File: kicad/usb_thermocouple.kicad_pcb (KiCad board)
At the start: 2 copper layers, 72 x 47.5 mm, 6 parts, among them U1 SeeeduinoXIAO, U2 ADA_MAX31855

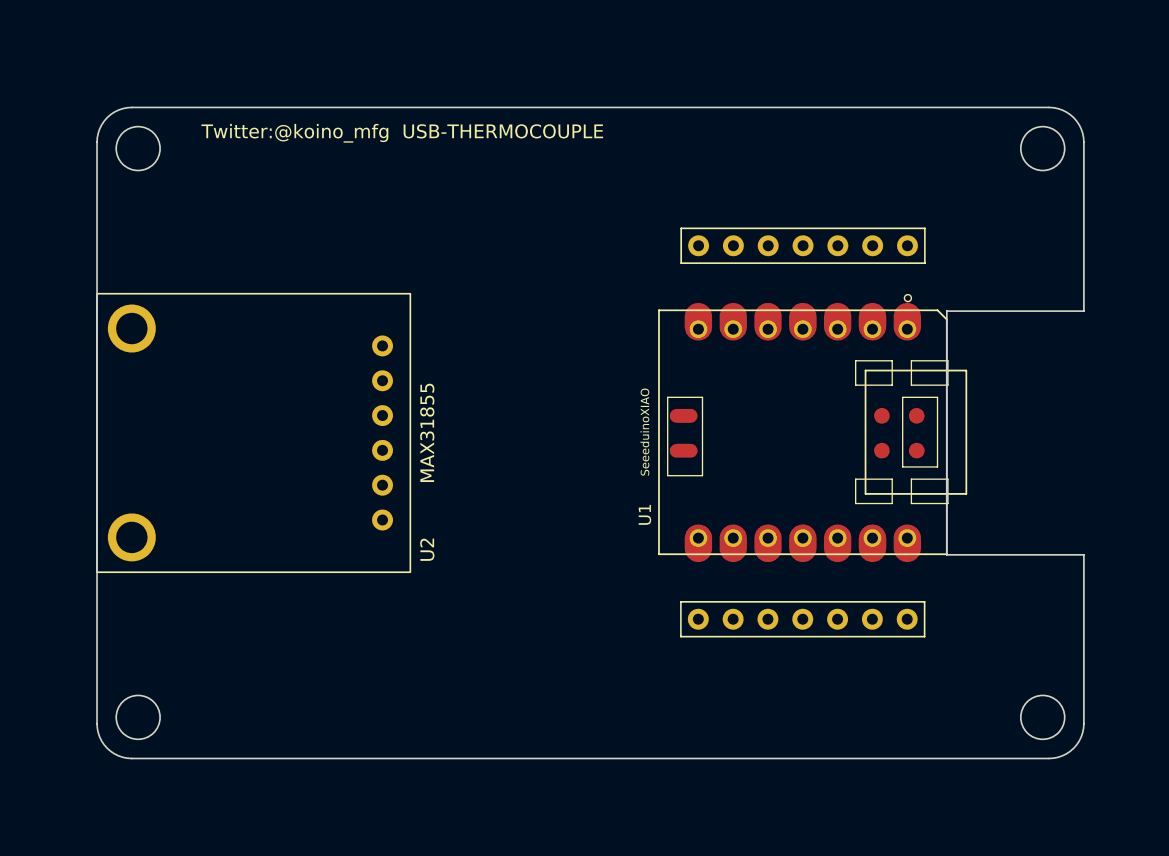
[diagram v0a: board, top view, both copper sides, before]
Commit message: 配線完了 DRC OK
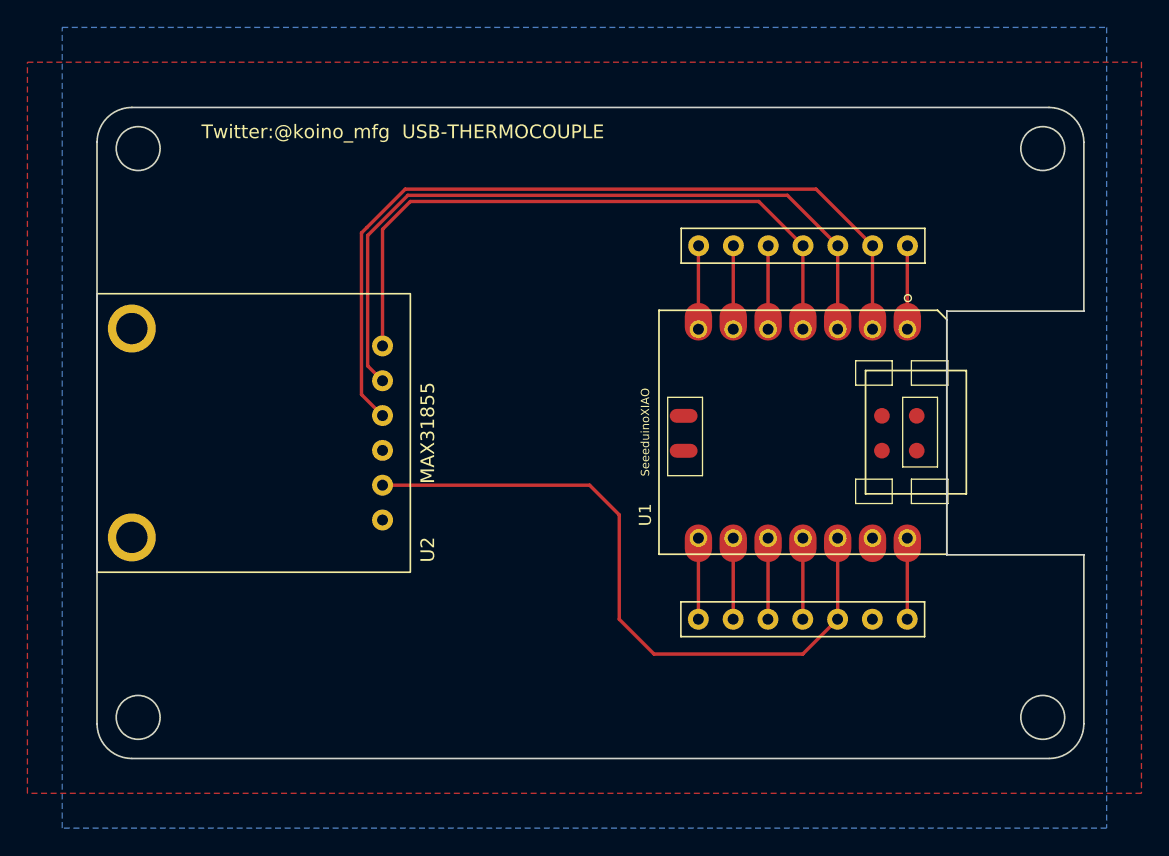
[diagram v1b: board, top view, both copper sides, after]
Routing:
- net Net-(U1-Pad2): track 0.00 -> 60.4 mm
- net Net-(U1-Pad3): track 0.00 -> 54.2 mm
- net Net-(U1-Pad12): track 0.00 -> 49.4 mm
- net Net-(U1-Pad4): track 0.00 -> 47.5 mm
- net Net-(U1-Pad7): track 0.00 -> 6.09 mm
- net Net-(U1-Pad6): track 0.00 -> 6.09 mm
- net Net-(U1-Pad5): track 0.00 -> 6.09 mm
- net Net-(U1-Pad1): track 0.00 -> 6.09 mm
- net Net-(U1-Pad9): track 0.00 -> 5.92 mm
- net Net-(U1-Pad8): track 0.00 -> 5.92 mm
- net Net-(U1-Pad11): track 0.00 -> 5.92 mm
- net Net-(U1-Pad10): track 0.00 -> 5.92 mm
- net Net-(U1-Pad14): track 0.00 -> 5.55 mm
- added copper zone on B.Cu, net GND
- added copper zone on F.Cu, net GND
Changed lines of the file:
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@@
       (net 20 "Net-(U1-Pad14)") (pintype "input"))
   )
+  (segment (start 20.83 -30.1) (end 20.83 -38.61) (width 0.25) (layer "F.Cu") (net 2))
+  (segment (start 20.83 -38.61) (end 22.86 -40.64) (width 0.25) (layer "F.Cu") (net 2))
+  (segment (start 22.86 -40.64) (end 48.28 -40.64) (width 0.25) (layer "F.Cu") (net 2))
+  (segment (start 48.28 -40.64) (end 51.51 -37.41) (width 0.25) (layer "F.Cu") (net 2))
+  (segment (start 51.498 -37.398) (end 51.51 -37.41) (width 0.25) (layer "F.Cu") (net 2))
+  (segment (start 51.498 -31.32) (end 51.498 -37.398) (width 0.25) (layer "F.Cu") (net 2))
+  (segment (start 48.958 -37.398) (end 48.97 -37.41) (width 0.25) (layer "F.Cu") (net 3))
+  (segment (start 48.958 -31.32) (end 48.958 -37.398) (width 0.25) (layer "F.Cu") (net 3))
+  (segment (start 46.418 -37.398) (end 46.43 -37.41) (width 0.25) (layer "F.Cu") (net 4))
+  (segment (start 46.418 -31.32) (end 46.418 -37.398) (width 0.25) (layer "F.Cu") (net 4))
+  (segment (start 20.83 -25.02) (end 19.293969 -26.556031) (width 0.25) (layer "F.Cu") (net 5))
+  (segment (start 56.578 -31.32) (end 56.578 -37.398) (width 0.25) (layer "F.Cu") (net 5))
+  (segment (start 52.46096 -41.53904) (end 56.59 -37.41) (width 0.25) (layer "F.Cu") (net 5))
+  (segment (start 22.487606 -41.53904) (end 52.46096 -41.53904) (width 0.25) (layer "F.Cu") (net 5))
+  (segment (start 19.293969 -38.345405) (end 19.684283 -38.735718) (width 0.25) (layer "F.Cu") (net 5))
+  (segment (start 19.684283 -38.735718) (end 22.487606 -41.53904) (width 0.25) (layer "F.Cu") (net 5))
+  (segment (start 19.293969 -26.556031) (end 19.293969 -38.345405) (width 0.25) (layer "F.Cu") (net 5))
+  (segment (start 56.578 -37.398) (end 56.59 -37.41) (width 0.25) (layer "F.Cu") (net 5))
+  (segment (start 43.878 -31.32) (end 43.878 -37.398) (width 0.25) (layer "F.Cu") (net 6))
+  (segment (start 43.878 -37.398) (end 43.89 -37.41) (width 0.25) (layer "F.Cu") (net 6))
+  (segment (start 50.37048 -41.08952) (end 54.05 -37.41) (width 0.25) (layer "F.Cu") (net 7))
+  (segment (start 54.038 -37.398) (end 54.05 -37.41) (width 0.25) (layer "F.Cu") (net 7))
+  (segment (start 54.038 -31.32) (end 54.038 -37.398) (width 0.25) (layer "F.Cu") (net 7))
+  (segment (start 19.743489 -38.159207) (end 22.673803 -41.08952) (width 0.25) (layer "F.Cu") (net 7))
+  (segment (start 22.673803 -41.08952) (end 50.37048 -41.08952) (width 0.25) (layer "F.Cu") (net 7))
+  (segment (start 20.83 -27.56) (end 19.743489 -28.646511) (width 0.25) (layer "F.Cu") (net 7))
+  (segment (start 19.743489 -28.646511) (end 19.743489 -38.159207) (width 0.25) (layer "F.Cu") (net 7))
+  (segment (start 59.118 -31.32) (end 59.118 -37.398) (width 0.25) (layer "F.Cu") (net 8))
+  (segment (start 59.118 -37.398) (end 59.13 -37.41) (width 0.25) (layer "F.Cu") (net 8))
+  (segment (start 43.877 -16.08) (end 43.877 -10.167) (width 0.25) (layer "F.Cu") (net 15))
+  (segment (start 43.877 -10.167) (end 43.87 -10.16) (width 0.25) (layer "F.Cu") (net 15))
+  (segment (start 46.417 -16.08) (end 46.417 -10.167) (width 0.25) (layer "F.Cu") (net 16))
+  (segment (start 46.417 -10.167) (end 46.41 -10.16) (width 0.25) (layer "F.Cu") (net 16))
+  (segment (start 48.957 -16.08) (end 48.957 -10.167) (width 0.25) (layer "F.Cu") (net 17))
+  (segment (start 48.957 -10.167) (end 48.95 -10.16) (width 0.25) (layer "F.Cu") (net 17))
+  (segment (start 51.497 -10.167) (end 51.49 -10.16) (width 0.25) (layer "F.Cu") (net 18))
+  (segment (start 51.497 -16.08) (end 51.497 -10.167) (width 0.25) (layer "F.Cu") (net 18))
+  (segment (start 54.03782 -15.70232) (end 54.03782 -10.16782) (width 0.25) (layer "F.Cu") (net 19))
+  (segment (start 38.1 -17.78) (end 38.1 -10.16) (width 0.25) (layer "F.Cu") (net 19))
+  (segment (start 35.94 -19.94) (end 38.1 -17.78) (width 0.25) (layer "F.Cu") (net 19))
+  (segment (start 38.1 -10.16) (end 40.64 -7.62) (width 0.25) (layer "F.Cu") (net 19))
+  (segment (start 40.64 -7.62) (end 51.49 -7.62) (width 0.25) (layer "F.Cu") (net 19))
+  (segment (start 51.49 -7.62) (end 54.03 -10.16) (width 0.25) (layer "F.Cu") (net 19))
+  (segment (start 20.83 -19.94) (end 35.94 -19.94) (width 0.25) (layer "F.Cu") (net 19))
+  (segment (start 54.03782 -10.16782) (end 54.03 -10.16) (width 0.25) (layer "F.Cu") (net 19))
+  (segment (start 59.11782 -15.70232) (end 59.11782 -10.16782) (width 0.25) (layer "F.Cu") (net 20))
+  (segment (start 59.11782 -10.16782) (end 59.11 -10.16) (width 0.25) (layer "F.Cu") (net 20))
+  (zone (net 1) (net_name "GND") (layer "F.Cu") (hatch edge 0.508)
+    (connect_pads (clearance 0.508))
+    (min_thickness 0.254) (filled_areas_thickness no)
+    (fill yes (thermal_gap 0.508) (thermal_bridge_width 0.508))
+    (polygon
+      (pts
+        (xy 76.2 2.54)
+        (xy -5.08 2.54)
+        (xy -5.08 -50.8)
+        (xy 76.2 -50.8)
+      )
+    )
+  )
+  (zone (net 1) (net_name "GND") (layer "B.Cu") (hatch edge 0.508)
+    (connect_pads (clearance 0.508))
+    (min_thickness 0.254) (filled_areas_thickness no)
+    (fill yes (thermal_gap 0.508) (thermal_bridge_width 0.508))
+    (polygon
+      (pts
+        (xy 73.66 5.08)
+        (xy -2.54 5.08)
+        (xy -2.54 -53.34)
+        (xy 73.66 -53.34)
+      )
+    )
+  )
 )
